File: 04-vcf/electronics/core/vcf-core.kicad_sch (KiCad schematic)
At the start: 7 parts, among them J1 Conn_01x06, J2 Conn_02x04_Counter_Clockwise, J3 Conn_02x02_Counter_Clockwise

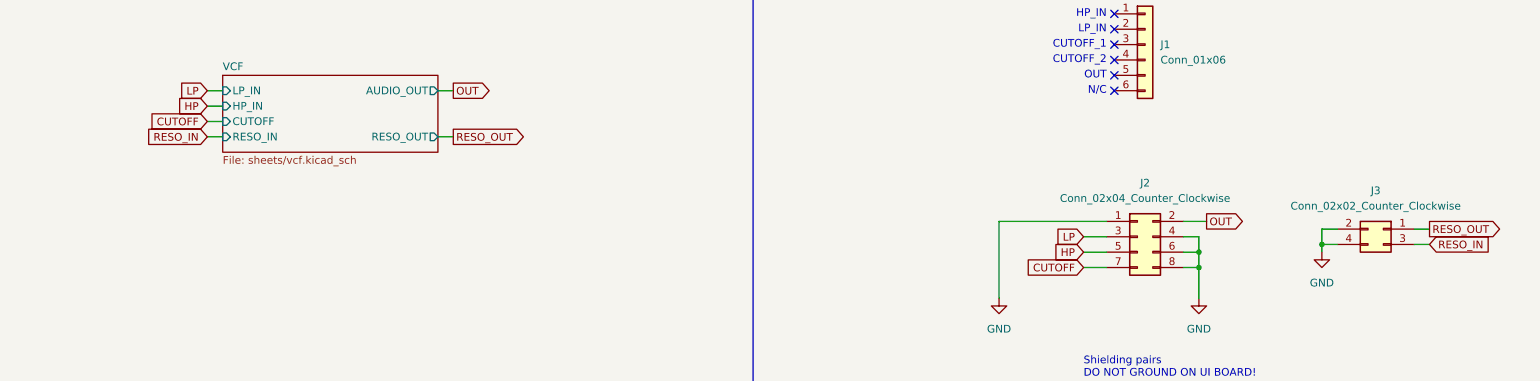
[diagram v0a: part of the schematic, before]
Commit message: Designed VCF UI board pre-check
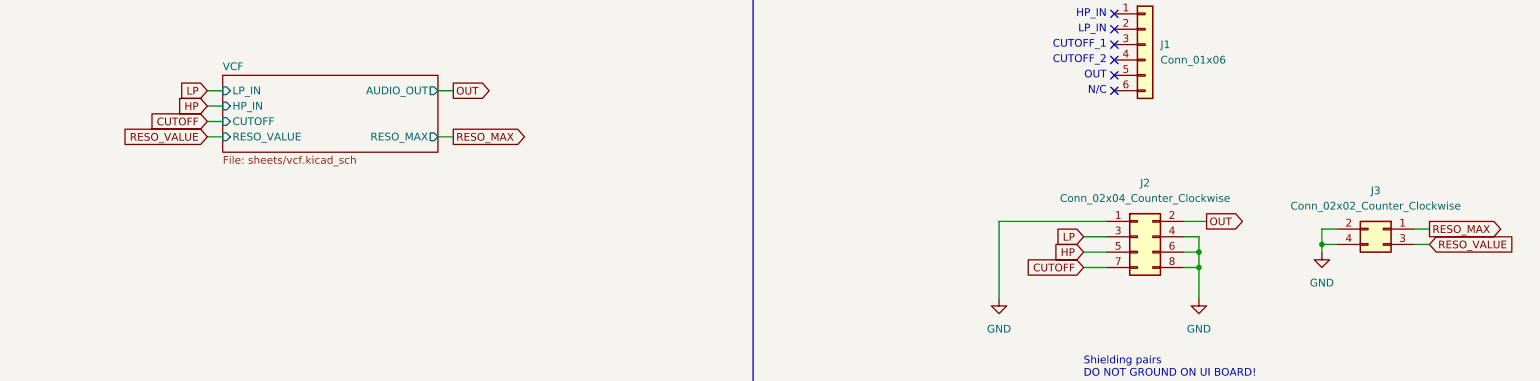
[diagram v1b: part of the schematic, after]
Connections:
- net RESO_IN renamed RESO_VALUE
- net RESO_OUT renamed RESO_MAX
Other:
- sheet VCF ports: added RESO_MAX, RESO_VALUE; removed RESO_IN, RESO_OUT
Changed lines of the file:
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@@
 		)
 	)
-	(global_label "RESO_IN"
+	(global_label "RESO_VALUE"
 		(shape input)
 		(at 60.96 86.36 180)
@@
 		)
 		(property "Intersheetrefs" "${INTERSHEET_REFS}"
-			(at 50.1129 86.36 0)
+			(at 46.3634 86.36 0)
 			(effects
 				(font
@@
 		)
 	)
-	(global_label "RESO_IN"
+	(global_label "RESO_VALUE"
 		(shape input)
 		(at 262.89 104.14 0)
@@
 		)
 		(property "Intersheetrefs" "${INTERSHEET_REFS}"
-			(at 273.7371 104.14 0)
-			(effects
-				(font
-					(size 1.27 1.27)
-				)
-				(justify left)
-				(hide yes)
-			)
-		)
-	)
-	(global_label "RESO_OUT"
+			(at 277.4866 104.14 0)
+			(effects
+				(font
+					(size 1.27 1.27)
+				)
+				(justify left)
+				(hide yes)
+			)
+		)
+	)
+	(global_label "RESO_MAX"
 		(shape output)
 		(at 262.89 101.6 0)
@@
 		)
 		(property "Intersheetrefs" "${INTERSHEET_REFS}"
-			(at 275.4304 101.6 0)
+			(at 275.5513 101.6 0)
 			(effects
 				(font
@@
 		)
 	)
-	(global_label "RESO_OUT"
+	(global_label "RESO_MAX"
 		(shape output)
 		(at 101.6 86.36 0)
@@
 		)
 		(property "Intersheetrefs" "${INTERSHEET_REFS}"
-			(at 114.1404 86.36 0)
+			(at 114.2613 86.36 0)
 			(effects
 				(font
@@
 			)
 		)
-		(pin "RESO_IN" input
+		(pin "RESO_MAX" output
+			(at 99.06 86.36 0)
+			(effects
+				(font
+					(size 1.27 1.27)
+				)
+				(justify right)
+			)
+		)
+		(pin "RESO_VALUE" input
 			(at 63.5 86.36 180)
 			(effects
@@
 			)
 		)
-		(pin "RESO_OUT" output
-			(at 99.06 86.36 0)
-			(effects
-				(font
-					(size 1.27 1.27)
-				)
-				(justify right)
-			)
-		)
 		(instances
-			(project "vcf"
+			(project "vcf-core"
 				(path "/8e2e31f3-eed5-4de1-966c-f4162758c735"
 					(page "3")
@@
 		)
 		(instances
-			(project "vcf"
+			(project "vcf-core"
 				(path "/8e2e31f3-eed5-4de1-966c-f4162758c735"
 					(page "4")

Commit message: Added production files to VCF core
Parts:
- H1, H2, H3, H4: Vendor (none) -> X
- J1: Mouser Part no. 474-PRT-09280 -> (none); Part no. (none) -> 474-PRT-09280
- J2: CHECKED (none) -> YES; Part URL (none) -> https://mou.sr/4nYsZDt; Part no. (none) -> 200-HTSW10407TD; Vendor (none) -> Mouser
- J3: Mouser Part no. 200-HTSW10207TD -> (none); Part no. (none) -> 200-HTSW10207TD
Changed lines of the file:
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@@
 			)
 		)
-		(property "Part No." ""
+		(property "Part URL" "https://mou.sr/4nYsZDt"
 			(at 214.63 102.87 0)
 			(effects
@@
 			)
 		)
-		(property "Part URL" ""
+		(property "Vendor" "Mouser"
 			(at 214.63 102.87 0)
 			(effects
@@
 			)
 		)
-		(property "Vendor" ""
+		(property "LCSC" ""
 			(at 214.63 102.87 0)
 			(effects
@@
 			)
 		)
-		(property "LCSC" ""
+		(property "Arwill" ""
+			(at 214.63 102.87 0)
+			(effects
+				(font
+					(size 1.27 1.27)
+				)
+				(hide yes)
+			)
+		)
+		(property "Hestore" ""
+			(at 214.63 102.87 0)
+			(effects
+				(font
+					(size 1.27 1.27)
+				)
+				(hide yes)
+			)
+		)
+		(property "CHECKED" "YES"
+			(at 214.63 102.87 0)
+			(effects
+				(font
+					(size 1.27 1.27)
+				)
+				(hide yes)
+			)
+		)
+		(property "Part no." "200-HTSW10407TD "
 			(at 214.63 102.87 0)
 			(effects
@@
 			)
 		)
-		(property "Mouser Part no." "200-HTSW10207TD"
+		(property "Arwill" ""
+			(at 255.27 101.6 0)
+			(effects
+				(font
+					(size 1.27 1.27)
+				)
+				(hide yes)
+			)
+		)
+		(property "Hestore" ""
+			(at 255.27 101.6 0)
+			(effects
+				(font
+					(size 1.27 1.27)
+				)
+				(hide yes)
+			)
+		)
+		(property "Part no." "200-HTSW10207TD"
 			(at 255.27 101.6 0)
 			(effects
@@
 			)
 		)
-		(property "Vendor" ""
+		(property "Vendor" "X"
 			(at 200.66 160.02 0)
 			(effects
@@
 		)
 		(property "CHECKED" "YES"
+			(at 200.66 160.02 0)
+			(effects
+				(font
+					(size 1.27 1.27)
+				)
+				(hide yes)
+			)
+		)
+		(property "Arwill" ""
+			(at 200.66 160.02 0)
+			(effects
+				(font
+					(size 1.27 1.27)
+				)
+				(hide yes)
+			)
+		)
+		(property "Hestore" ""
 			(at 200.66 160.02 0)
 			(effects
@@
 			)
 		)
-		(property "Vendor" ""
+		(property "Vendor" "X"
 			(at 179.07 160.02 0)
 			(effects
@@
 		)
 		(property "CHECKED" "YES"
+			(at 179.07 160.02 0)
+			(effects
+				(font
+					(size 1.27 1.27)
+				)
+				(hide yes)
+			)
+		)
+		(property "Arwill" ""
+			(at 179.07 160.02 0)
+			(effects
+				(font
+					(size 1.27 1.27)
+				)
+				(hide yes)
+			)
+		)
+		(property "Hestore" ""
 			(at 179.07 160.02 0)
 			(effects
@@
 			)
 		)
-		(property "Mouser Part no." "474-PRT-09280"
+		(property "Arwill" ""
+			(at 215.9 71.12 0)
+			(effects
+				(font
+					(size 1.27 1.27)
+				)
+				(hide yes)
+			)
+		)
+		(property "Hestore" ""
+			(at 215.9 71.12 0)
+			(effects
+				(font
+					(size 1.27 1.27)
+				)
+				(hide yes)
+			)
+		)
+		(property "Part no." "474-PRT-09280"
 			(at 215.9 71.12 0)
 			(effects
@@
 			)
 		)
-		(property "Vendor" ""
+		(property "Vendor" "X"
 			(at 220.98 160.02 0)
 			(effects
@@
 		)
 		(property "CHECKED" "YES"
+			(at 220.98 160.02 0)
+			(effects
+				(font
+					(size 1.27 1.27)
+				)
+				(hide yes)
+			)
+		)
+		(property "Arwill" ""
+			(at 220.98 160.02 0)
+			(effects
+				(font
+					(size 1.27 1.27)
+				)
+				(hide yes)
+			)
+		)
+		(property "Hestore" ""
 			(at 220.98 160.02 0)
 			(effects
@@
 			)
 		)
-		(property "Vendor" ""
+		(property "Vendor" "X"
 			(at 241.3 160.02 0)
 			(effects
@@
 			(at 241.3 160.02 0)
 			(effects
+				(font
+					(size 1.27 1.27)
+				)
+				(hide yes)
+			)
+		)
+		(property "Arwill" ""
+			(at 241.3 160.02 0)
+			(effects
+				(font
+					(size 1.27 1.27)
+				)
+				(hide yes)
+			)
+		)
+		(property "Hestore" ""
+			(at 241.3 160.02 0)
+			(effects

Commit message: Fixed VCF v0.1 bugs - new version: v0.2
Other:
- company: (none) -> Shmøergh
- title: (none) -> Hog Moduleur VCF
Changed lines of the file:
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@@
 	(generator_version "9.0")
 	(paper "A4")
+	(title_block
+		(title "Hog Moduleur VCF")
+		(date "2025-07-31")
+		(rev "v0.2")
+		(company "Shmøergh")
+	)
 	(text "Power"
 		(exclude_from_sim no)

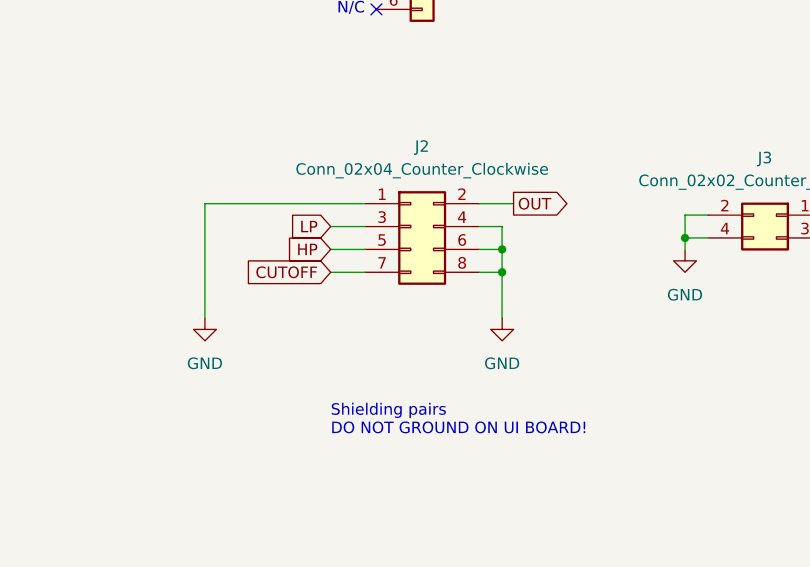
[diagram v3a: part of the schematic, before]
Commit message: Redesigned VCF PCB to avoid crosstalk
- There's been quite a bit of crosstalk between the input and output of the VCF module. This PCB design attemtps to separate the input and output so that the crosstalk is minimized.
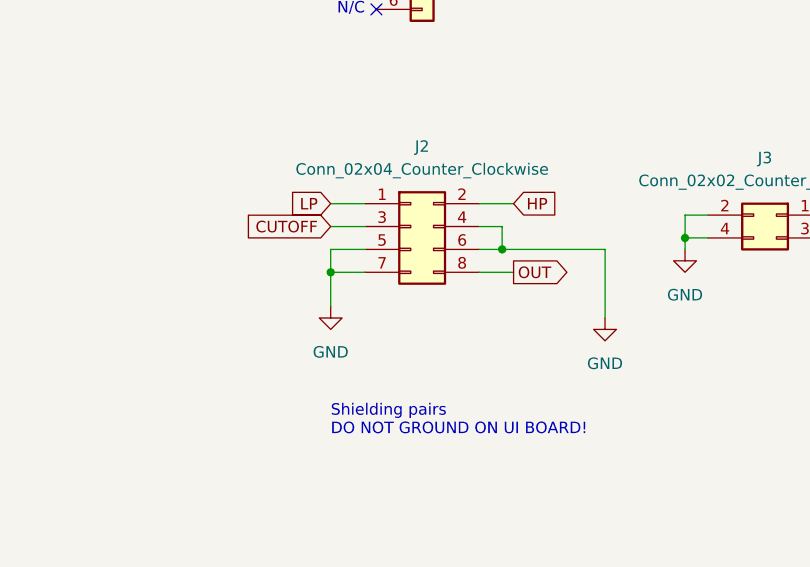
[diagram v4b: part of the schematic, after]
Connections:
- net CUTOFF: now also J2.3 (Pin_3); no longer J2.7 (Pin_7)
- net GND: now also J2.5 (Pin_5), J2.7 (Pin_7); no longer J2.1 (Pin_1), J2.8 (Pin_8)
- net HP: now also J2.2 (Pin_2); no longer J2.5 (Pin_5)
- net LP: now also J2.1 (Pin_1); no longer J2.3 (Pin_3)
- net OUT: now also J2.8 (Pin_8); no longer J2.2 (Pin_2)
